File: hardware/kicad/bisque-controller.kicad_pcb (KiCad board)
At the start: 4 copper layers, 100 x 100 mm, 143 parts, among them J1 USB-C, J10 AUX, J11 INPUTS, J12 CT, J13 AC_SENSE_DNP, J14 QWIIC, J2 5V_IN, J3 TC1_K, J4 SSR1, J5 DISPLAY, J6 NAV_SW, J7 AUX, J8 TC2_K, J9 SSR2, Q2 AO3400A, Q3 AO3400A, Q4 AO3401A, Q5 AO3400A, Q6 AO3400A, SW1 RESET, SW2 BOOT, U1 ESP32-S3-WROOM-1U-N16R2, U2 AMS1117-3.3, U3 MAX31856MUD+, U4 SRV05-4, U5 MAX31856MUD+, U6 ULN2003A, U7 ADE7953ACPZ, Y1 3.579545MHz XO

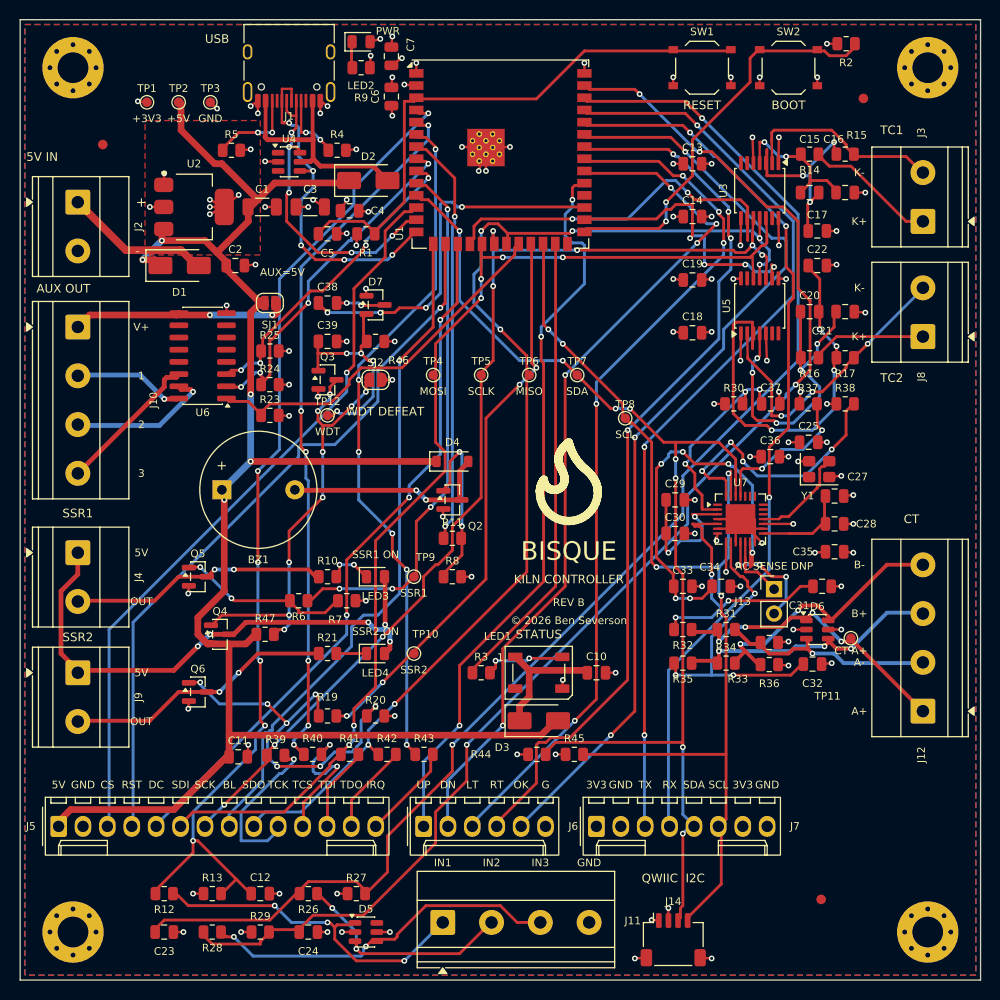
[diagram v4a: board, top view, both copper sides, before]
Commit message: wip(hw): watchdog one-shot + multi-unit schematic support
CHECKPOINT, NOT FAB-READY. Two gates are red and the fab outputs in
jlcpcb/ and gerbers/ are deliberately NOT regenerated, so they still
describe the old charge-pump board. Do not order from this tree.

  make pcb-build       5 unconnected pads (was 0/0 before this)
  pcb-check-portable   4 symbol/symbol collisions (was 0)

What is finished and verified:

Multi-unit symbol support. KiCad splits 74xGxx across two units - logic on
1, GND/VCC on 2 - and gen_sch.py emitted "(unit 1)" only, so a part like
that would have silently shipped with no power pins. COMPONENTS now
expands to one entry per placeable unit ("U10#1", "U10#2"); a single-unit
part keeps its own designator as the key and unit_view() hands back the
symbol unchanged, so the other 140 parts take the same path they always
did. Proven: the refactor reproduced the committed schematic byte for
byte before any new part was added, and kicad-cli's own netlist export
resolves U10 to ONE component carrying all eight pins.

check_sch_layout.py was the other half and was missing. It boxed a placed
symbol with lib_body_box() keyed on lib_id, i.e. every unit's body and
pins unioned into one rectangle, which then swallowed the part's own
fields and the power ports beside it - 10 phantom collisions. It reads the
placed "(unit N)" now. That fix also exposed a real bug in units_of():
inside lib_symbols the parent carries the full lib_id while its children
keep the bare name, so anchoring the sub-symbol regex on the parent found
nothing and every symbol read as single-unit. Matched on the suffix now.

The circuit: D7/C38/C39/R46 (BAT54S clamp-and-peak-detector) out,
U10 SN74LVC1G123 retriggerable one-shot in, with R46 100k + C38 22uF
setting a 1.65-2.71 s worst-case window and R48 holding B low while the
MCU is high-Z. Q3, Q4, R47 and SJ2 untouched. Rationale, the arithmetic
that condemns the pump, and the rejected supervisor ICs are all in
design.py's watchdog block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
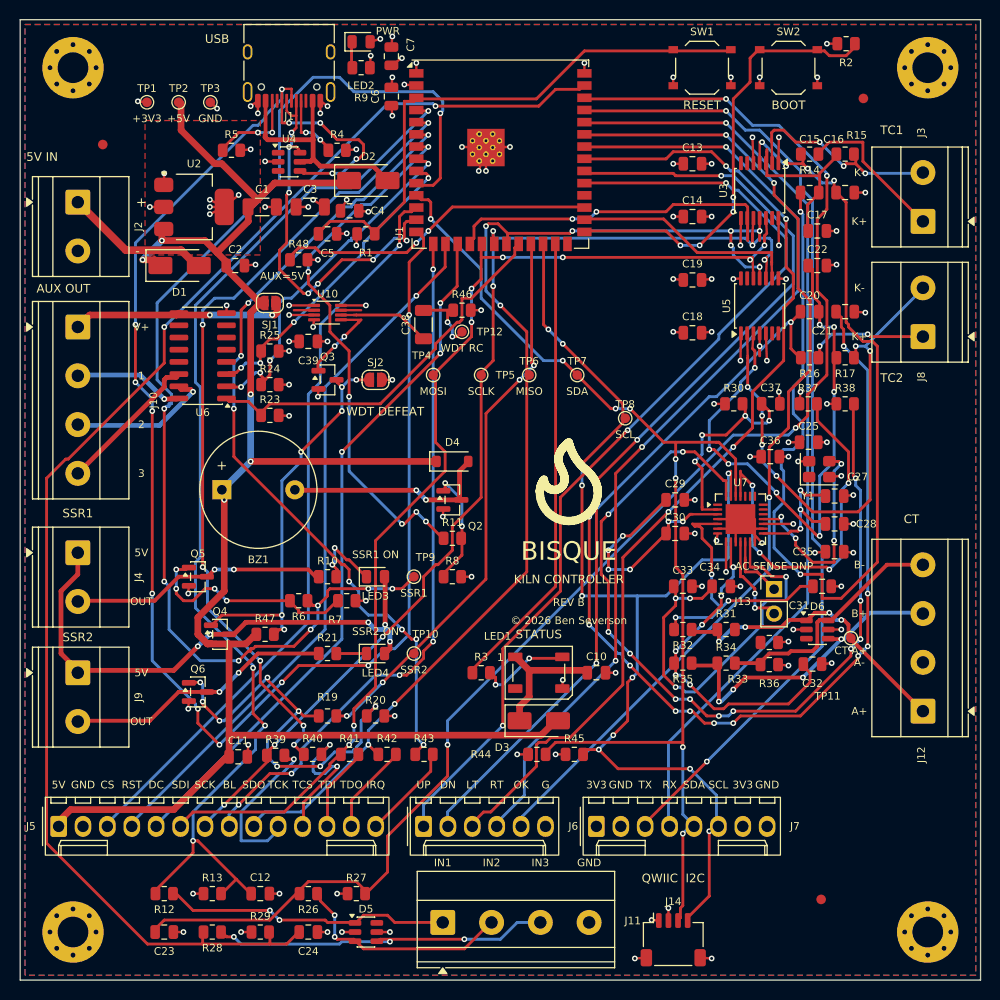
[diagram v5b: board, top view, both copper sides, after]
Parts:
- removed D7: BAT54S, SOT-23
- added R48: 100k, R_0805_2012Metric, F.Cu at (49.0, 45.0)
- added U10: SN74LVC1G123, VSSOP-8_2.3x2mm_P0.5mm, F.Cu at (52.0, 50.5)
- C38: value 100nF -> 22uF; footprint C_0805_2012Metric -> C_1206_3216Metric
- C39: value 1uF -> 100nF
- R46: value 1M -> 100k
- moved TP12 16.5 mm to (66.0, 52.5)
- moved C38 10.2 mm to (62.0, 51.8), turned to 90 degrees
- moved R46 9.57 mm to (66.0, 50.2)
- moved C39 2.00 mm to (50.0, 53.5)
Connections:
- C38 pad 1: WDT_KICK -> WDT_CT_N
- C38 pad 2: WDT_PUMP -> WDT_CT_P
- C39 pad 1: WDT_HOLD -> +3V3
- Q3 pad 1: WDT_HOLD -> WDT_OK
- R46 pad 1: WDT_HOLD -> WDT_CT_P
- R46 pad 2: GND -> +3V3
- TP12 pad 1: WDT_HOLD -> WDT_CT_P
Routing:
- net USB_DP: track 36.3 -> 169.6 mm, vias 5 -> 14
- net TC1_P_F: track 15.3 -> 111.6 mm, vias 2 -> 6
- net TC2_P_F: track 34.7 -> 123.1 mm, vias 5 -> 13
- net SSR1_CTRL: track 56.7 -> 124.4 mm, vias 4 -> 8
- net ADE_CS: track 28.0 -> 89.1 mm, vias 4 -> 12
- net TC2_N: track 31.3 -> 54.9 mm, vias 3 -> 6
- net ADE_SCLK: track 15.8 -> 39.4 mm, vias 2 -> 4
- net BTN_UP: track 76.8 -> 100.3 mm
- net WDT_HOLD: track 23.4 -> 0.00 mm, vias 4 -> 0
- net CTA_N: track 22.7 -> 0.00 mm, vias 1 -> 0
- net TC2_N_F: track 44.3 -> 60.6 mm, vias 4 -> 8
- net T_IRQ: track 71.5 -> 85.3 mm, vias 6 -> 8
- net ALARM: track 43.3 -> 56.3 mm, vias 2 -> 6
- net BTN_LEFT: track 91.4 -> 103.7 mm, vias 5 -> 4
- net ADE_CLKIN: track 10.5 -> 22.2 mm, vias 0 -> 4
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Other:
- board text added: "WDT RC"
- board text removed: "WDT"

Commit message: feat(hw): the watchdog becomes a specified one-shot, and floorplan.py works again
Replaces the BAT54S diode charge pump with U10, an SN74LVC1G123
retriggerable monostable (TI, SSOP-8, C123302). Board is 0 DRC / 0
unconnected / 0 footprint errors and all twelve checkers pass; fab
outputs and 3D renders regenerated.

WHY THE PUMP HAD TO GO. Solving its steady state exactly gives 0.63 V of
gate drive at the 5 Hz kick against the AO3400A's 1.45 V threshold -- and
0.84 V even in the typical corner, below the TYPICAL 1.0 V threshold. The
sizing note it replaces computed the decay constant (R46*C39 = 1 s) and
the gate margin but never the replenishment constant (R46*C38 = 0.1 s),
and flagged its own values as unverified because "no target kick
frequency or hold-decay spec exists yet". A faster kick rescues the
voltage but not the temperature: Schottky reverse leakage sits IN the
timing path and roughly doubles per 10 C, so the budget for a transient
firmware stall falls from 0.31 s at 25 C to 0.11 s at 60 C and vanishes
near 85 C, next to a 5 kW heat source. No passive value fixes a leak that
is the timer. Off-the-shelf supervisors (TPS3823, STWD100) were evaluated
and rejected on output shape: they emit a fixed reset PULSE per timeout,
leaving the heat rail energised 75-95% of the time under dead firmware.
They exist to reboot MCUs; gating a rail needs a level.

Window is 1.65-2.71 s worst case over -40..125 C, every term a datasheet
or purchase-tolerance figure, against a 5 Hz kick -- 8.3x margin.

PACKAGE. SSOP-8, not the VSSOP-8 the same die also ships in. VSSOP's
0.5 mm land leaves 0.150 mm between pads against this board's 0.200 mm
rule: twelve DRC violations before a single track is routed. SSOP-8 gives
0.350 mm. It is also the same TI die as the datasheet the window
arithmetic came from (SCES586E), which a Nexperia part would not have
been -- that would have left the window quoted from the wrong spec.

FLOORPLAN. floorplan.py could not run at all: missing FID1-FID3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
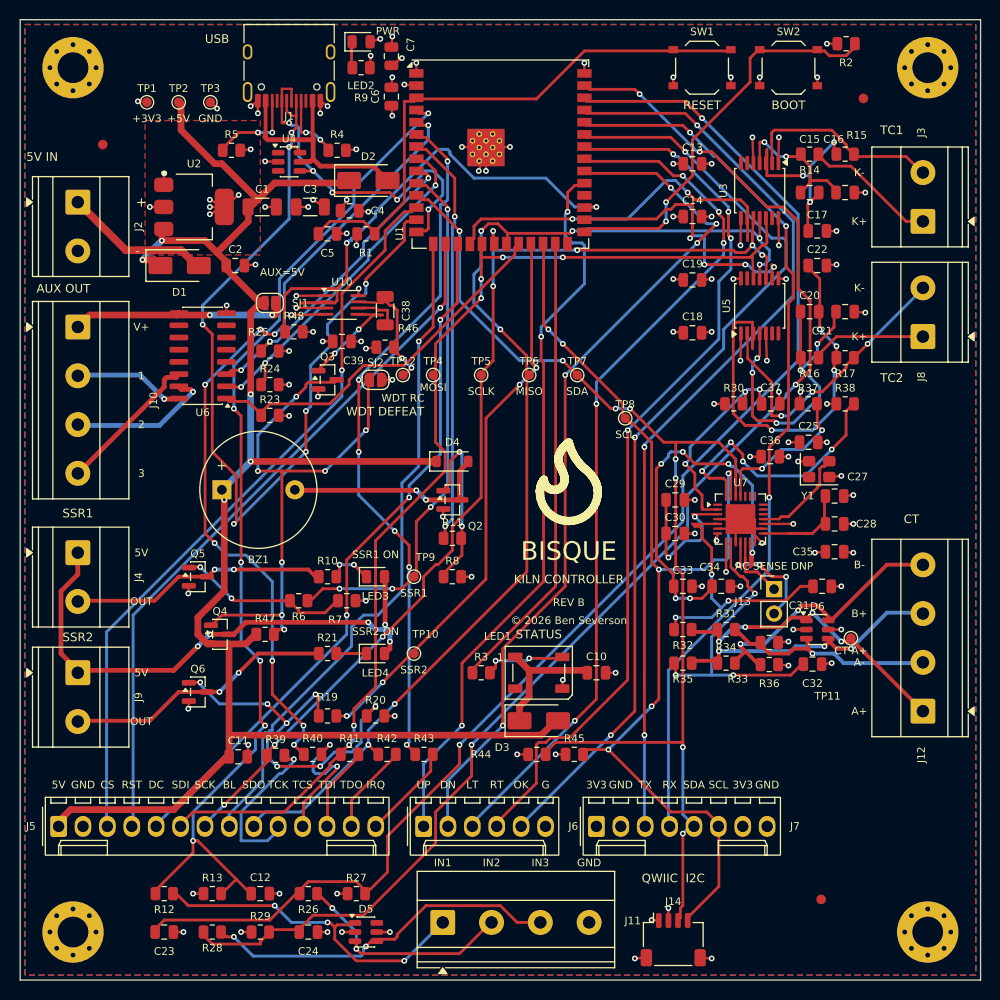
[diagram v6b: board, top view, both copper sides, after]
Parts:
- U10: footprint VSSOP-8_2.3x2mm_P0.5mm -> SSOP-8_2.95x2.8mm_P0.65mm
- moved R46 8.88 mm to (58.0, 54.1)
- moved TP12 7.62 mm to (59.9, 57.0)
- moved R48 7.52 mm to (48.5, 52.5)
- moved C38 4.25 mm to (58.0, 50.3)
- moved C39 3.50 mm to (53.5, 53.5)
- moved U10 1.70 mm to (53.5, 49.7)
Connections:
- R46 pad 1: WDT_CT_P -> +3V3
- R46 pad 2: +3V3 -> WDT_CT_P
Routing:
- net USB_DP: track 169.6 -> 38.1 mm, vias 14 -> 5
- net TC1_P_F: track 111.6 -> 15.3 mm, vias 6 -> 2
- net TC2_P_F: track 123.1 -> 34.7 mm, vias 13 -> 5
- net SSR1_CTRL: track 124.4 -> 56.7 mm, vias 8 -> 4
- net ADE_CS: track 89.1 -> 28.0 mm, vias 12 -> 4
- net USB_DN: track 42.2 -> 94.0 mm
- net TC2_N: track 54.9 -> 31.3 mm, vias 6 -> 3
- net ADE_SCLK: track 39.4 -> 15.8 mm, vias 4 -> 2
- net BTN_UP: track 100.3 -> 76.8 mm
- net CTA_N: track 0.00 -> 22.7 mm, vias 0 -> 1
- net WDT_KICK: track 35.7 -> 56.8 mm
- net SSR_PG: track 41.1 -> 58.5 mm, vias 6 -> 7
- net TC2_N_F: track 60.6 -> 44.3 mm, vias 8 -> 4
- net ALARM: track 56.3 -> 43.3 mm, vias 6 -> 2
- net BTN_LEFT: track 103.7 -> 91.4 mm, vias 4 -> 5
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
